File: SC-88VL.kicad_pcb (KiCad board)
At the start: 2 copper layers, 77.5 x 64.8 mm, 14 parts

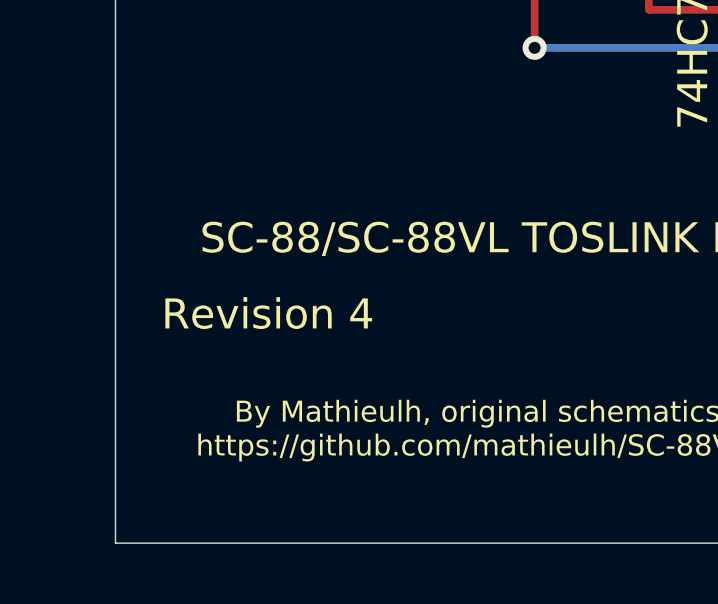
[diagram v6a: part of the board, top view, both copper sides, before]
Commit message: Changed revision on silkscreen
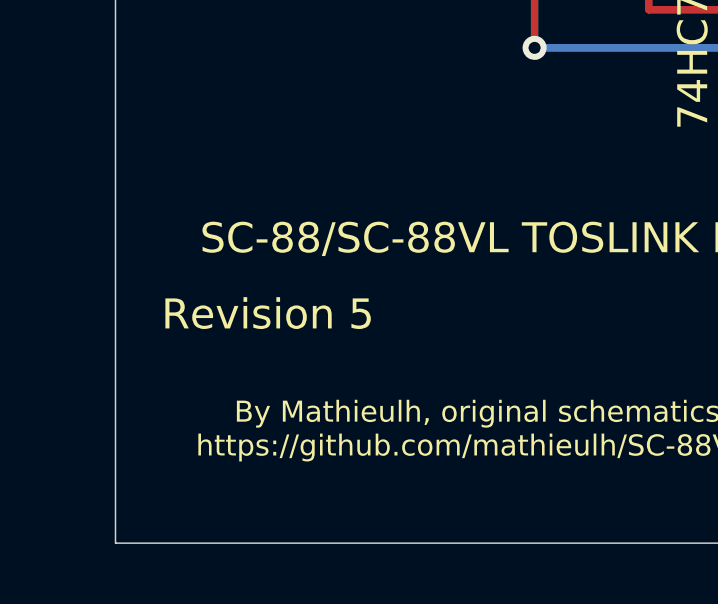
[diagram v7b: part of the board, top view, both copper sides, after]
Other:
- board text added: "Revision 5"
- board text removed: "Revision 4"
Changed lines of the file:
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@@
     (effects (font (size 1 1) (thickness 0.25)))
   )
-  (gr_text "Revision 4" (at 69.85 90.17) (layer F.SilkS)
+  (gr_text "Revision 5" (at 69.85 90.17) (layer F.SilkS)
     (effects (font (size 1 1) (thickness 0.25)))
   )
